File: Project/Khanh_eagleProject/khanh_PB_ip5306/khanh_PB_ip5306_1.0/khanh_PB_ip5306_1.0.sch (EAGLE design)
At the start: 18 parts

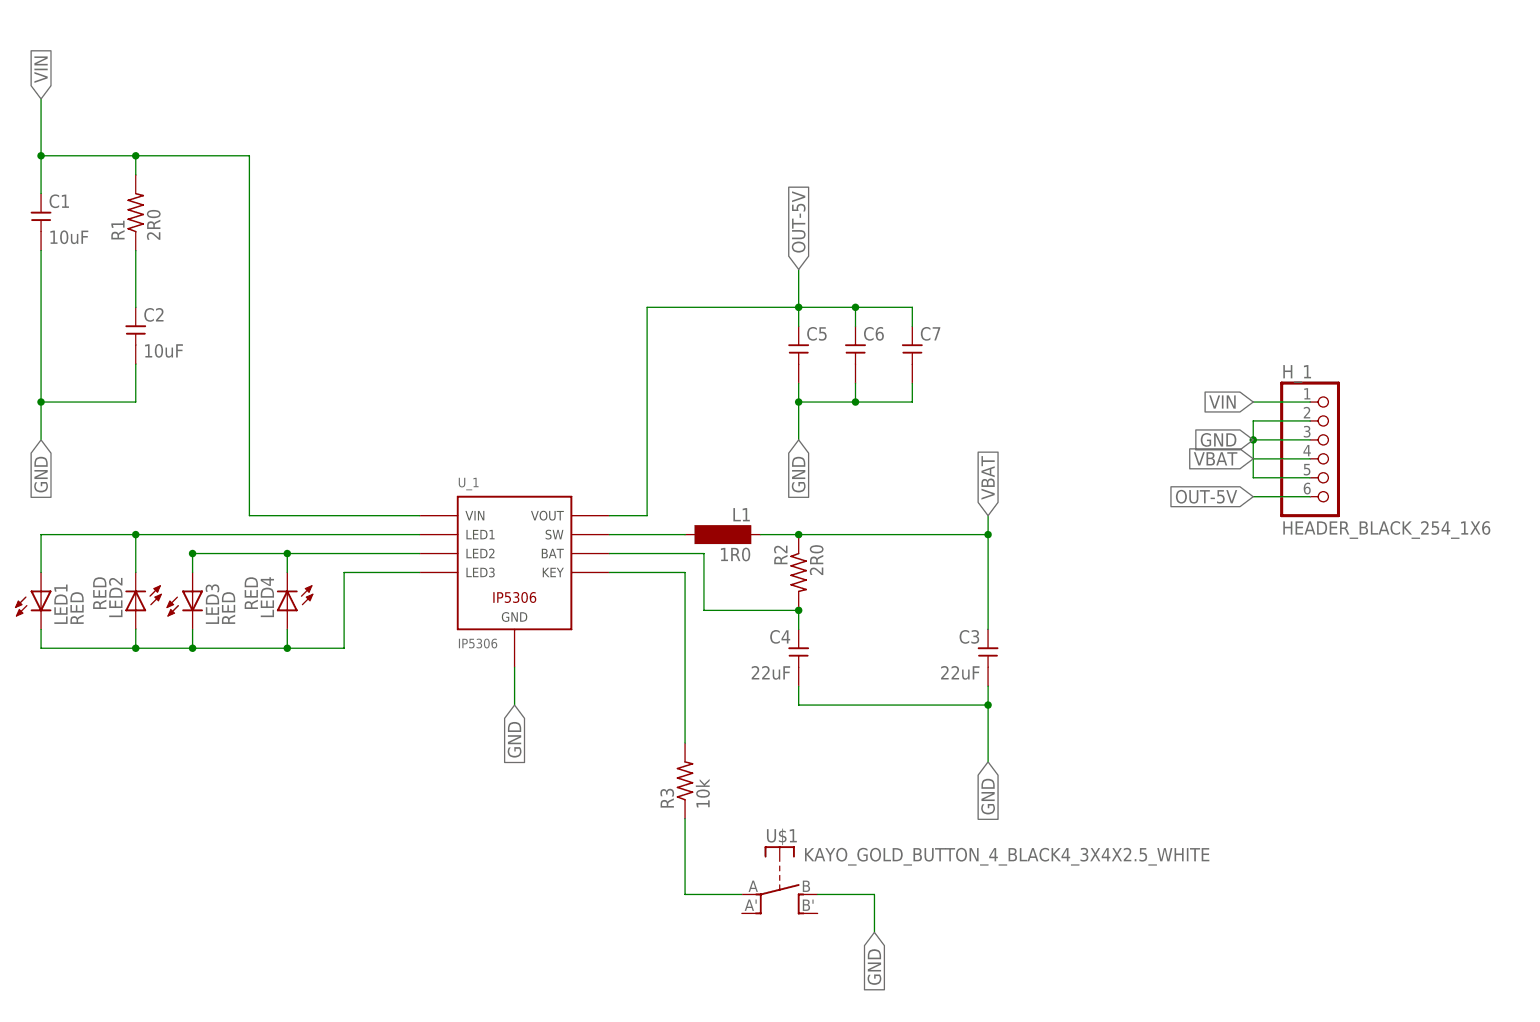
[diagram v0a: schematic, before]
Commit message: chỉnh sửa pcd mạch sạc ip5306
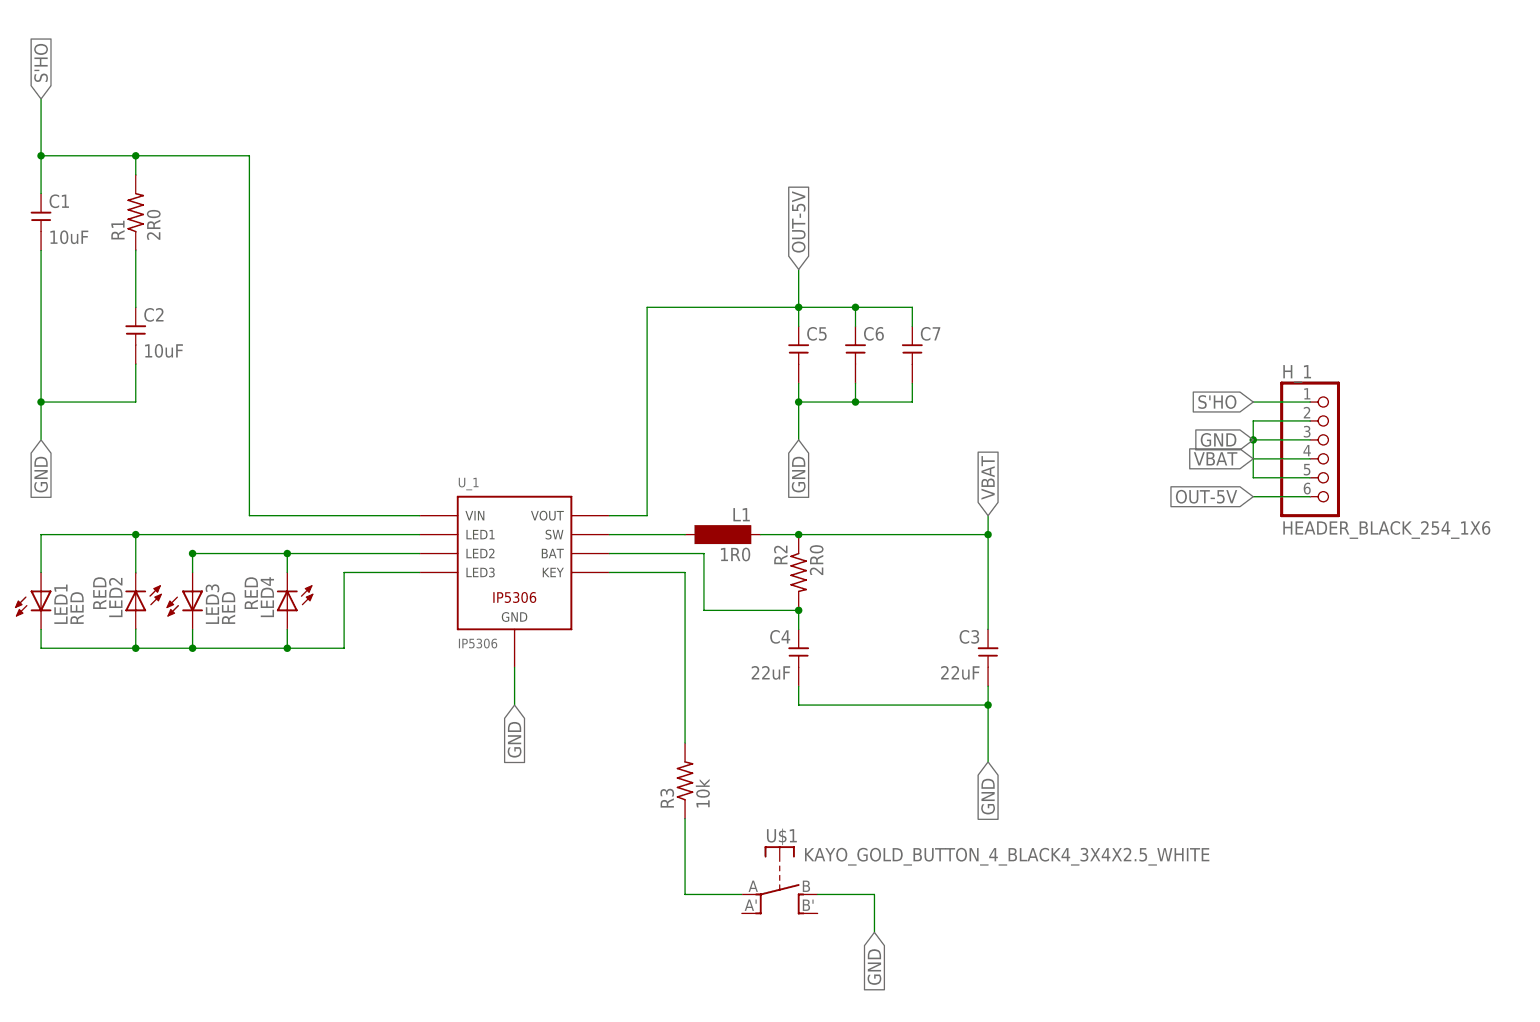
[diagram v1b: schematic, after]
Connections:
- net VIN renamed S'HO
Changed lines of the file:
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@@
 </busses>
 <nets>
-<net name="VIN" class="0">
+<net name="S'HO" class="0">
 <segment>
 <pinref part="U_1" gate="G$1" pin="P$1"/>
